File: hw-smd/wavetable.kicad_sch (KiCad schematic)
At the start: 32 parts, among them J8 SJ1-3535NG-GR (green), J9 Waveblaster 2x13 male, U11 NE5532, U12 74LVC2G06

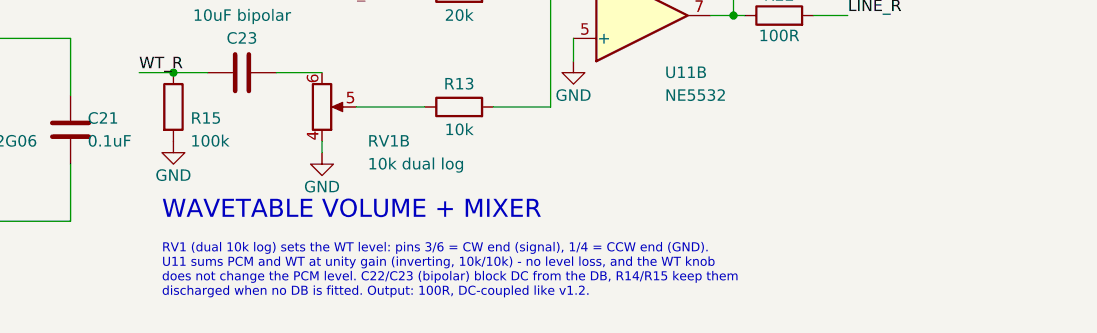
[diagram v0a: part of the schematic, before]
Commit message: Mixer docs: schematic note, DAC load and wording for the +6 dB WT gain
Review fixes for e33fce5:
- The wavetable-sheet note (both boards, and the schematic PDFs) still said
  "unity gain (inverting, 10k/10k)". It now gives PCM 20k/20k (~unity) and
  WT x2 (+6 dB), wrapped so it stays clear of the THT spare U7 gates.
- THT README: the PCM510x now sees ~20.5k (R7 + R10), not ~10.5k.
- Wording: the 47p corner is ~170 kHz (was ~160 kHz with 10k/100p), PCM gain
  moves -0.4 -> -0.2 dB ("essentially unchanged"), and keeping 100p costs
  ~0.2 dB more at 20 kHz. Same wording in the BOM notes.

Co-Authored-By: Claude Opus 5.5 <noreply@anthropic.com>
Claude-Session: https://claude.ai/code/session_011utN3x8yYUNDvkpGCEq5yD
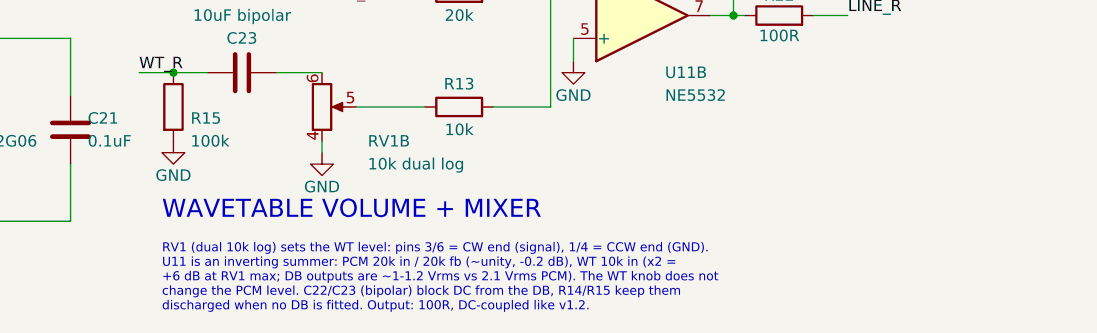
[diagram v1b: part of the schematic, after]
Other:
- note added: "RV1 (dual 10k log) sets the WT level: pins 3/6 = CW end (signal), 1/4 = CCW end (GND). U11 is an inverting summer: PCM 20k in / 20k fb (~unity, -0.2 dB), WT 10k in (x2 = +6 dB at RV1 max; DB outputs are ~1-1.2 Vrms vs 2.1 Vrms PCM). The WT knob does not change the PCM level. C22/C23 (bipolar) block DC from the DB, R14/R15 keep them discharged when no DB is fitted. Output: 100R, DC-coupled like v1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"
- note removed: "RV1 (dual 10k log) sets the WT level: pins 3/6 = CW end (signal), 1/4 = CCW end (GND). U11 sums PCM and WT at unity gain (inverting, 10k/10k) - no level loss, and the WT knob does not change the PCM level. C22/C23 (bipolar) block DC from the DB, R14/R15 keep them discharged when no DB is fitted. Output: 100R, DC-coupled like v1.2."
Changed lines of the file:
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@@
 		)
 	)
-	(text "RV1 (dual 10k log) sets the WT level: pins 3/6 = CW end (signal), 1/4 = CCW end (GND).\nU11 sums PCM and WT at unity gain (inverting, 10k/10k) - no level loss, and the WT knob\ndoes not change the PCM level. C22/C23 (bipolar) block DC from the DB, R14/R15 keep them\ndischarged when no DB is fitted. Output: 100R, DC-coupled like v1.2."
+	(text "RV1 (dual 10k log) sets the WT level: pins 3/6 = CW end (signal), 1/4 = CCW end (GND).\nU11 is an inverting summer: PCM 20k in / 20k fb (~unity, -0.2 dB), WT 10k in (x2 =\n+6 dB at RV1 max; DB outputs are ~1-1.2 Vrms vs 2.1 Vrms PCM). The WT knob does not\nchange the PCM level. C22/C23 (bipolar) block DC from the DB, R14/R15 keep them\ndischarged when no DB is fitted. Output: 100R, DC-coupled like v1.2."
 		(exclude_from_sim no)
 		(at 134.62 154.94 0)
